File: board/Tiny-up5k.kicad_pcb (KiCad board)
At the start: 2 copper layers, 17.8 x 35.6 mm, 37 parts, among them J1 CONN_01X14, J2 CONN_01X14, J5 Prog, SW1 SW_Push, U1 ICE40UP5K-SG48ITR, U2 MIC5504-3.3YM5, U3 DSC6001CI2A-016.0000T, U4 MIC5504-1.2YM5, U5 AT25xxx-MA, U6 USB_OTG

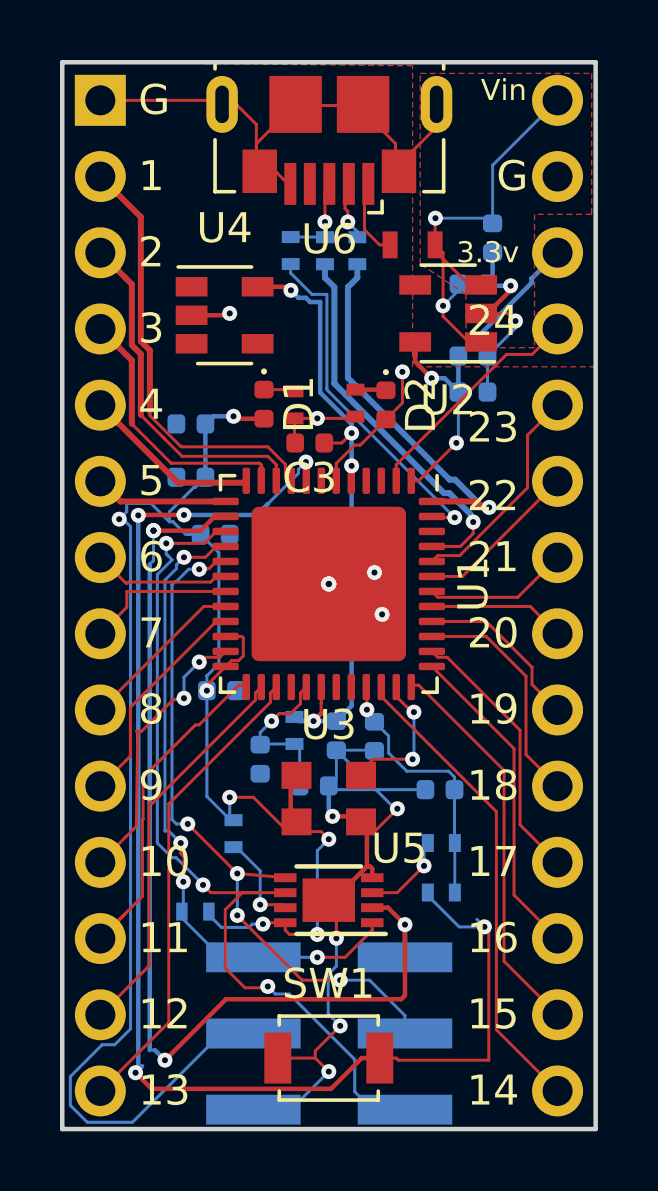
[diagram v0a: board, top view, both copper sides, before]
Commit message: Added more part numbers for the components. Changed the footprint of 5v capacitor (make it bigger) to accomodate for the bigger value.
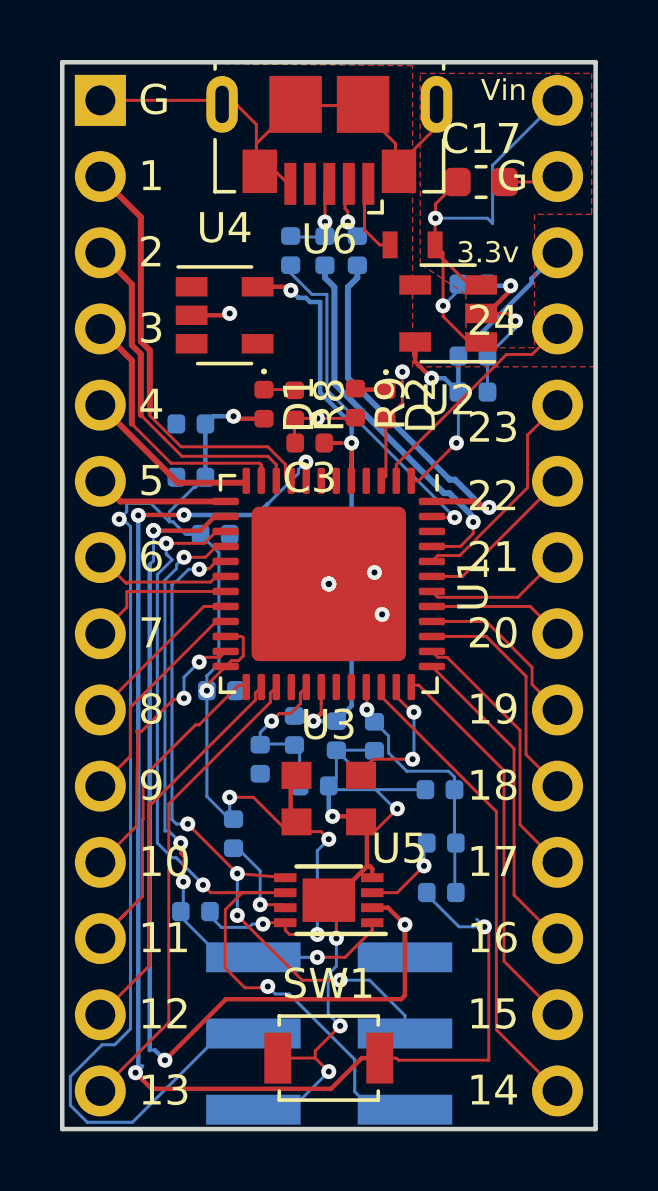
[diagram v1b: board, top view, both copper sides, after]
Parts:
- C17: footprint Capacitor_SMD:C_0402_1005Metric -> Capacitor_SMD:C_0603_1608Metric; moved to F.Cu
- R1, R10, R2, R3, R4, R5, R7, R8, R9: footprint Resistors_SMD:R_0402_NoSilk -> Resistor_SMD:R_0402_1005Metric
- R6: value R -> 10k; footprint Resistors_SMD:R_0402 -> Resistor_SMD:R_0402_1005Metric
- moved C17 1.90 mm to (156.2, 100.5), turned to 0 degrees
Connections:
- U1 pad 3: (no net) -> LED
- U1 pad 6: LED -> (no net)
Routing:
- net +5V: track 15.1 -> 16.6 mm
- net VCC_CORE: track 21.2 -> 22.4 mm, vias 4 -> 3
- net GND: track 56.3 -> 57.3 mm
- net LED: track 4.72 -> 3.92 mm
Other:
- board text added: "3V3"
- board text added: "SDI"
- board text added: "SDO"
- board text removed: "IO0"
- board text removed: "IO1"

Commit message: 0x01
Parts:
- moved L1 0.42 mm to (154.3, 102.4)
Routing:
- net GND: track 57.3 -> 65.7 mm
- net +5V: track 16.6 -> 9.21 mm, vias 2 -> 1
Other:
- board text added: "Tiny-up5k 0x01"

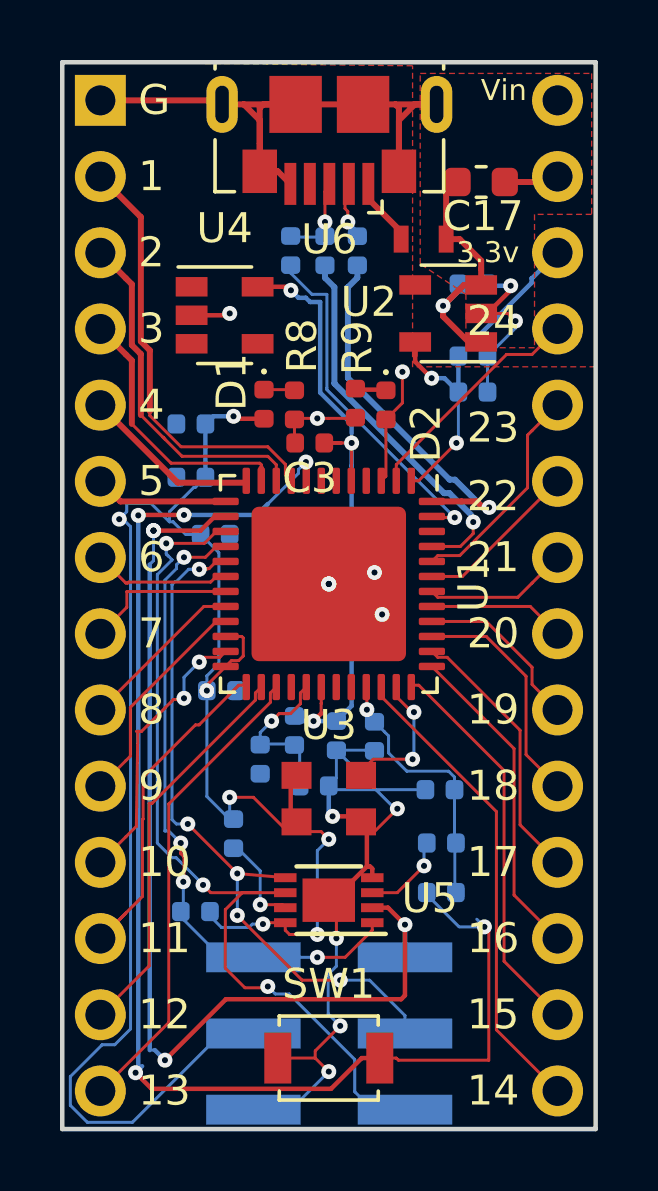
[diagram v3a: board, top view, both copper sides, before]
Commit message: Increase the spacing between the leds and their resistor.
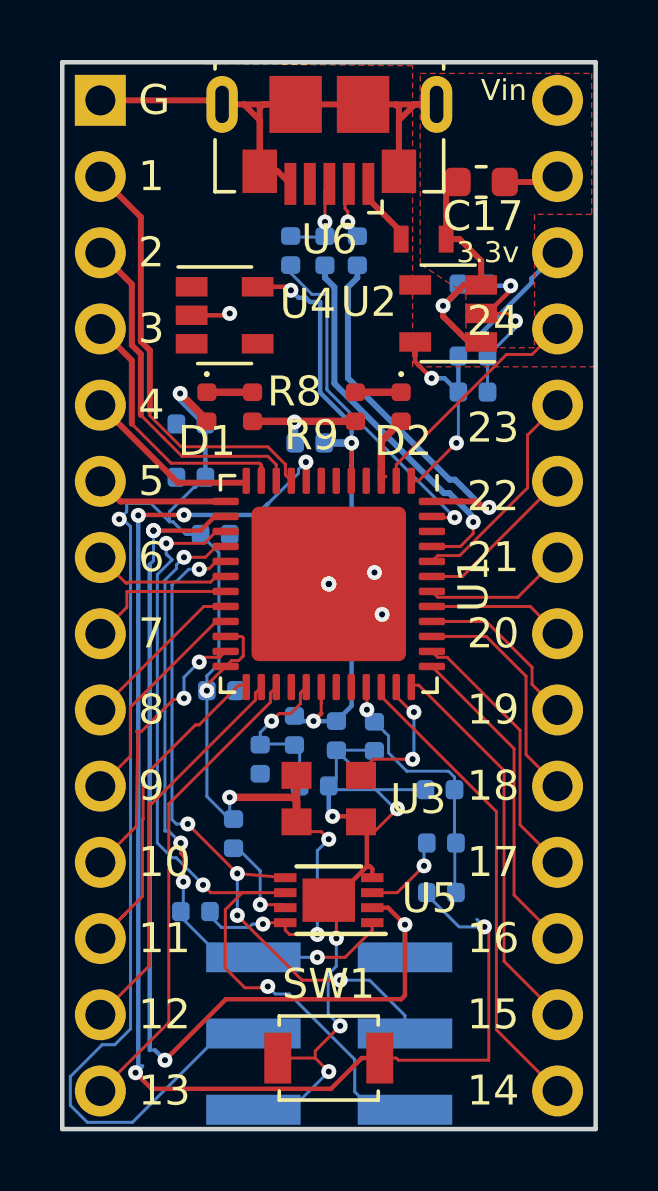
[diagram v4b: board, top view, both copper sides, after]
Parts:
- C3: moved to B.Cu
- moved D1 1.91 mm to (147.1, 108.0)
- moved R8 1.40 mm to (148.6, 108.0)
- moved D2 0.51 mm to (153.5, 108.0)
- moved R9 0.12 mm to (152.0, 108.0)
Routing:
- net LED: track 3.92 -> 2.48 mm, vias 1 -> 0
- net GND: track 65.7 -> 67.1 mm
- net VCC_CORE: track 22.4 -> 21.8 mm
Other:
- board text added: "Tiny-up5k"
- board text removed: "Tiny-up5k 0x01"

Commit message: change j5 footprint for default kicad footprint
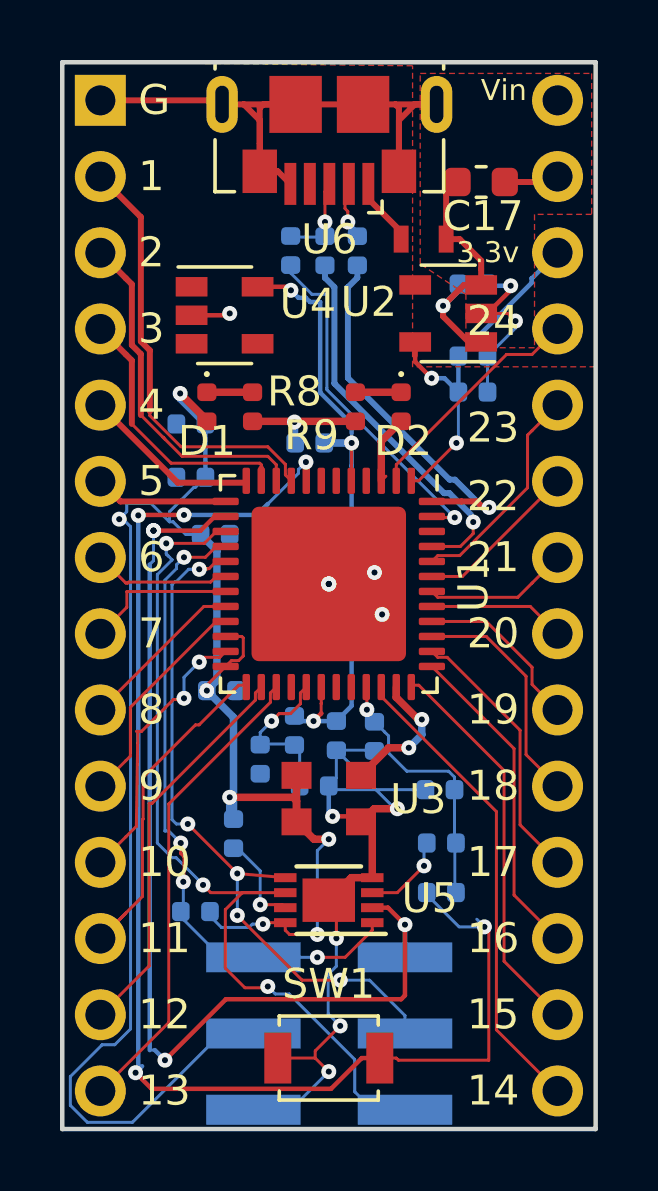
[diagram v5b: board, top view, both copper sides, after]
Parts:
- J5: footprint Pin_Headers:Pin_Header_Straight_2x03_Pitch2.54mm_SMD -> Connector_PinHeader_2.54mm:PinHeader_2x03_P2.54mm_Vertical_SMD
- R8, R9: value 270 -> 680
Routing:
- net GND: track 67.1 -> 67.9 mm
- net CLK: track 4.38 -> 4.97 mm

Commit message: Improve the frabrication layout. Make some trace wider
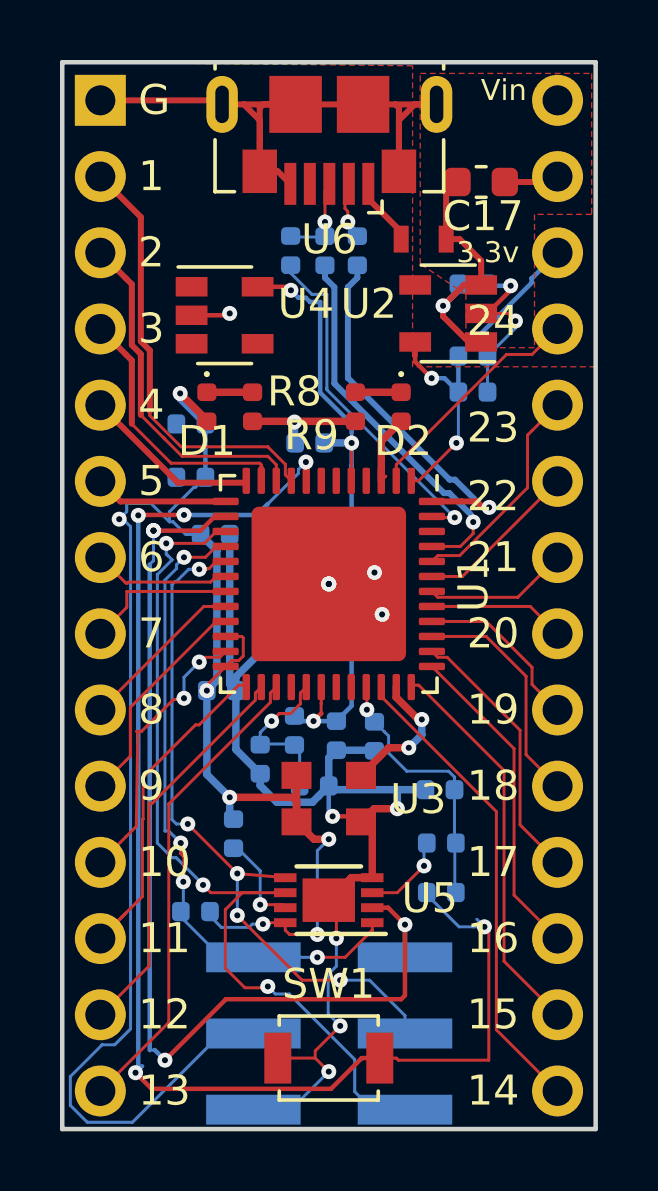
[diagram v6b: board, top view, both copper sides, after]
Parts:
- U5: value AT25xxx-MA -> SST25VF016B
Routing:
- net GND: track 67.9 -> 82.2 mm
- net SPI_VCCIO1: track 88.4 -> 87.6 mm

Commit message: Replaced footprint of spi flash chip
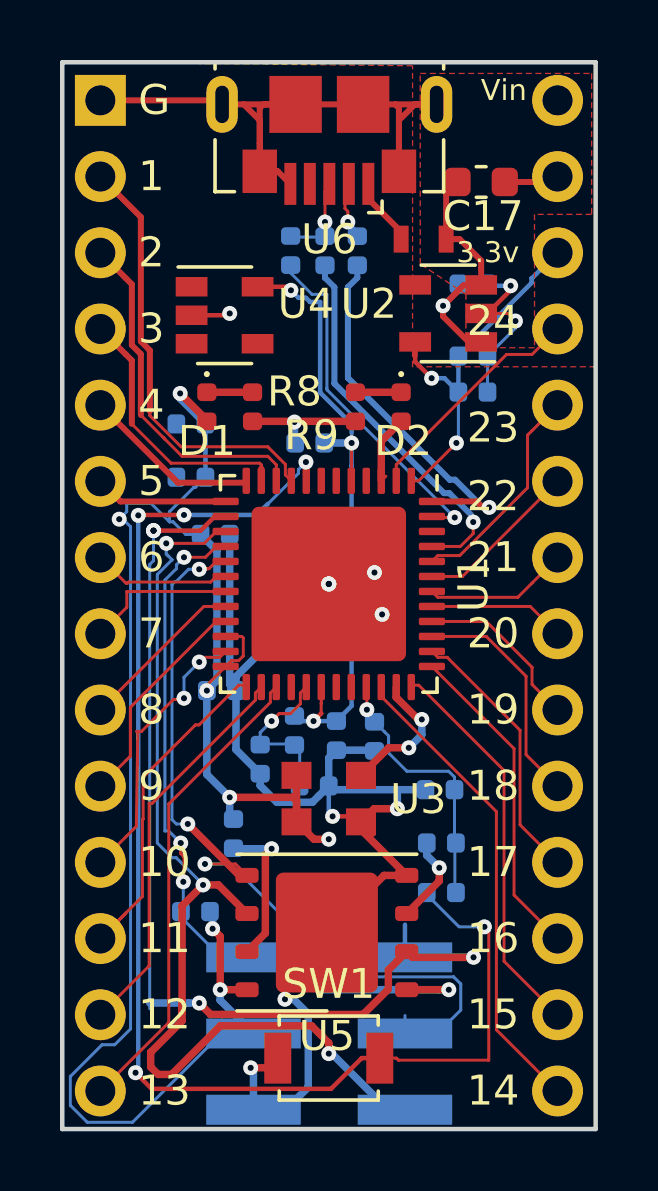
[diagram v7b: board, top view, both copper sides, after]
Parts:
- U5: footprint Package_DFN_QFN:DFN-8-1EP_3x2mm_P0.5mm_EP1.75x1.45mm -> Package_SON:WSON-8-1EP_6x5mm_P1.27mm_EP3.4x4mm
- moved U5 1.08 mm to (151.1, 125.5)
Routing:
- net SCK: track 29.5 -> 35.3 mm
- net GND: track 82.2 -> 87.4 mm, vias 13 -> 12
- net SDO: track 23.9 -> 28.7 mm, vias 5 -> 3
- net SS: track 21.8 -> 25.5 mm
- net SPI_VCCIO1: track 87.6 -> 85.7 mm
- net Net-(R7-Pad2): track 3.22 -> 5.15 mm
- net CRESET_B: track 45.3 -> 44.6 mm
